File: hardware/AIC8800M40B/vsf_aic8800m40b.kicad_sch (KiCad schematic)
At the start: 87 parts, among them J1 USB_A, J2 USB_C_Receptacle_USB2.0, J3 USB_C_Receptacle_USB2.0, J4 Micro_SD_Card_Det1, J6 Conn_Coaxial, J7 Conn_Coaxial, J8 Conn_02x15_Odd_Even, Q1 S9013, SW1 SW_Push, SW2 SW_Push, SW3 SW_Push, SW4 SW_Push, U1 AIC8800MX0_48P, U2 CH340N, U3 ETA9638, U4 ETA3486, Y1 40M, 10PPM,10pF

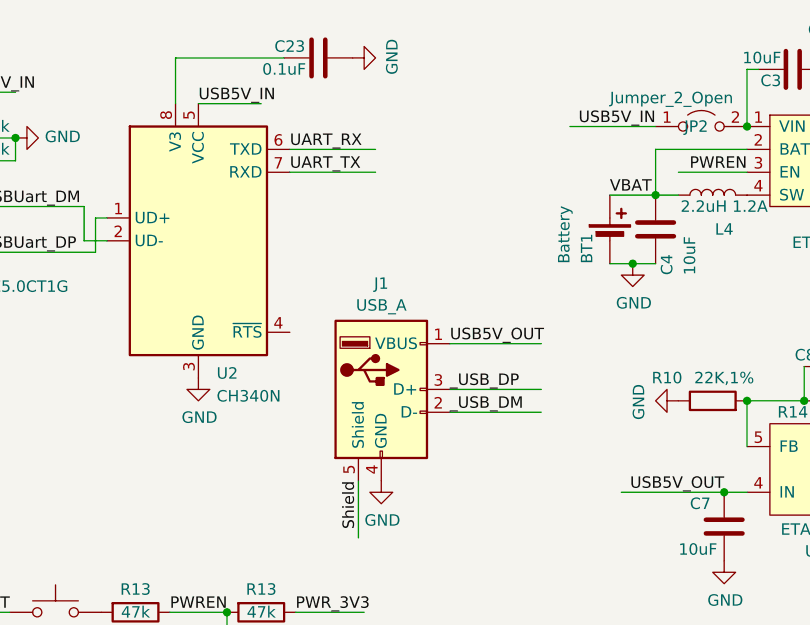
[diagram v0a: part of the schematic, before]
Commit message: [hardware/aic8800m40b] add level converter for debug uart
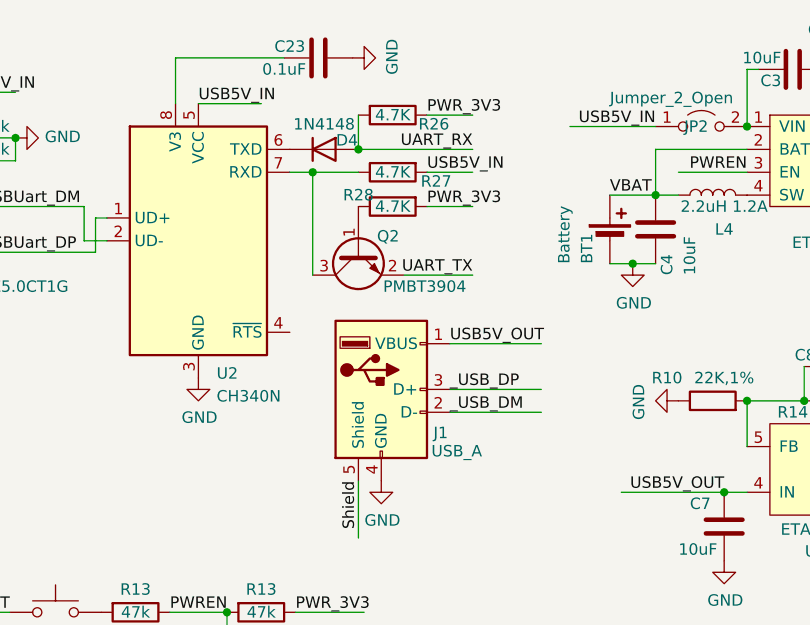
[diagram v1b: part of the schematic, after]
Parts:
- added D4: 1N4148, Diode_SMD:D_SOD-523, symbol Diode:1N4148
- added Q2: PMBT3904, Package_TO_SOT_SMD:SOT-23, symbol Device:Q_NPN_BEC
- added R26, R27, R28: 4.7K, Resistor_SMD:R_0402_1005Metric, symbol Device:R
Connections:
- net GPIOA8: now also D4.2 (A), R26.2; no longer U2.6 (TXD)
- net GPIOA9: now also Q2.2 (E); no longer U2.7 (RXD)
- net PWR_3V3: now also R26.1, R28.2
- net USB5V_IN: now also R27.2
- new net: Q2.3 (C), R27.1, U2.7 (RXD)
- new net: Q2.1 (B), R28.1
- new net: D4.1 (K), U2.6 (TXD)

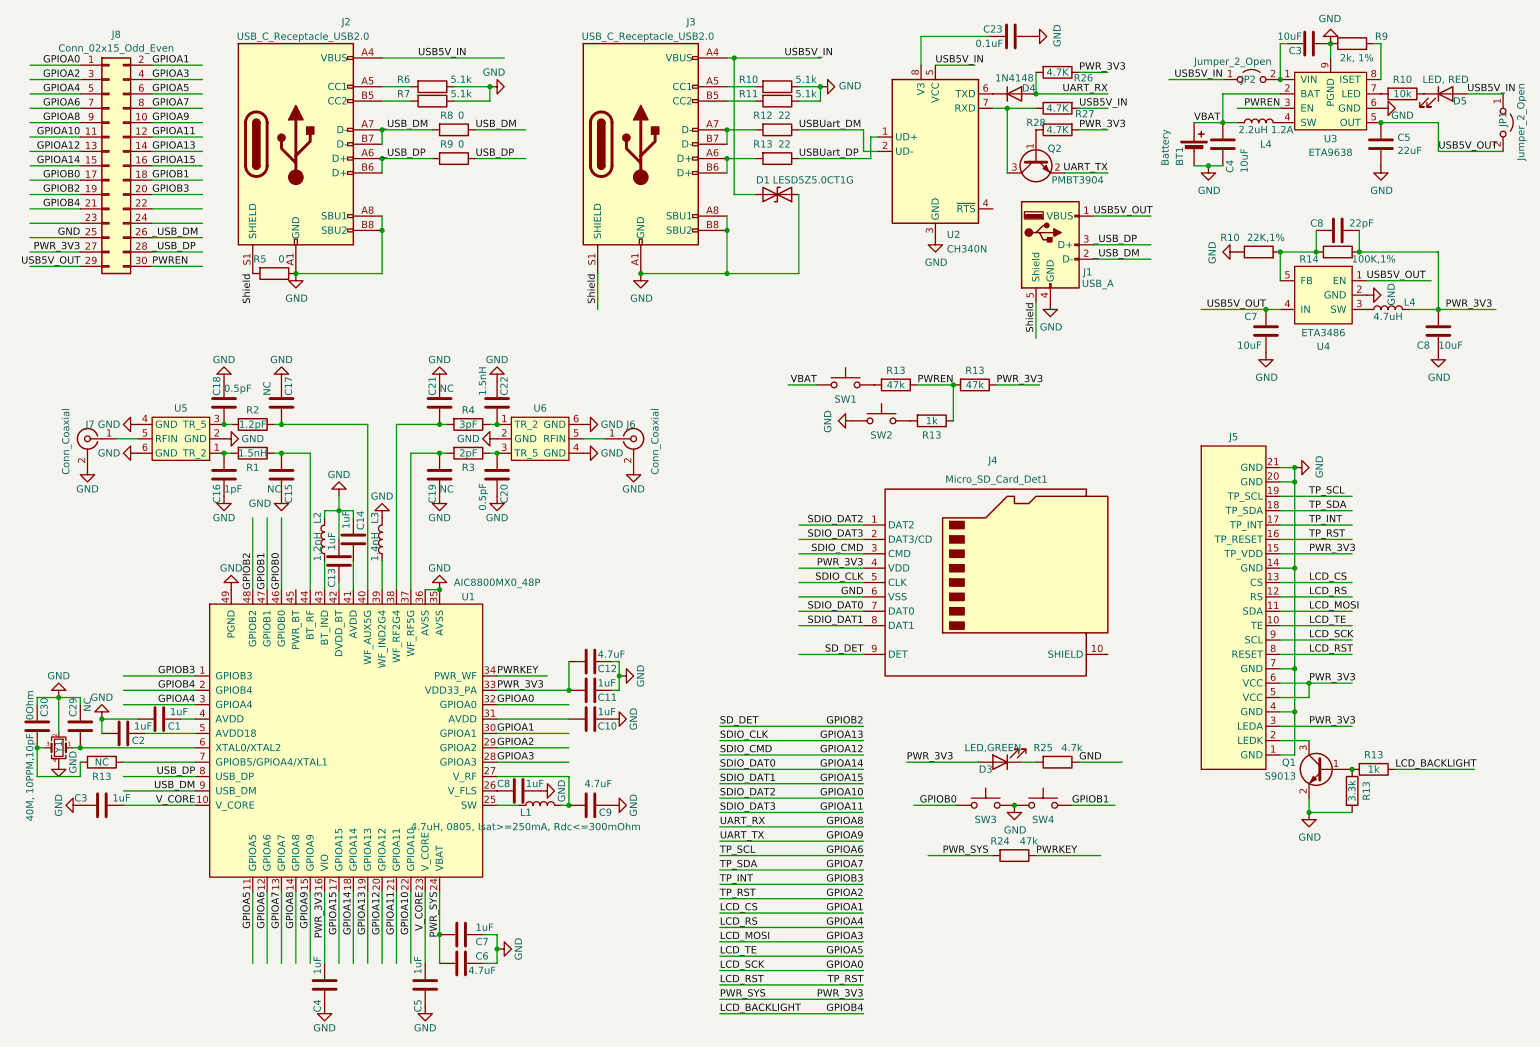
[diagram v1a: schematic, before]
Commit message: [hardware/aic8800m40b] fix typo
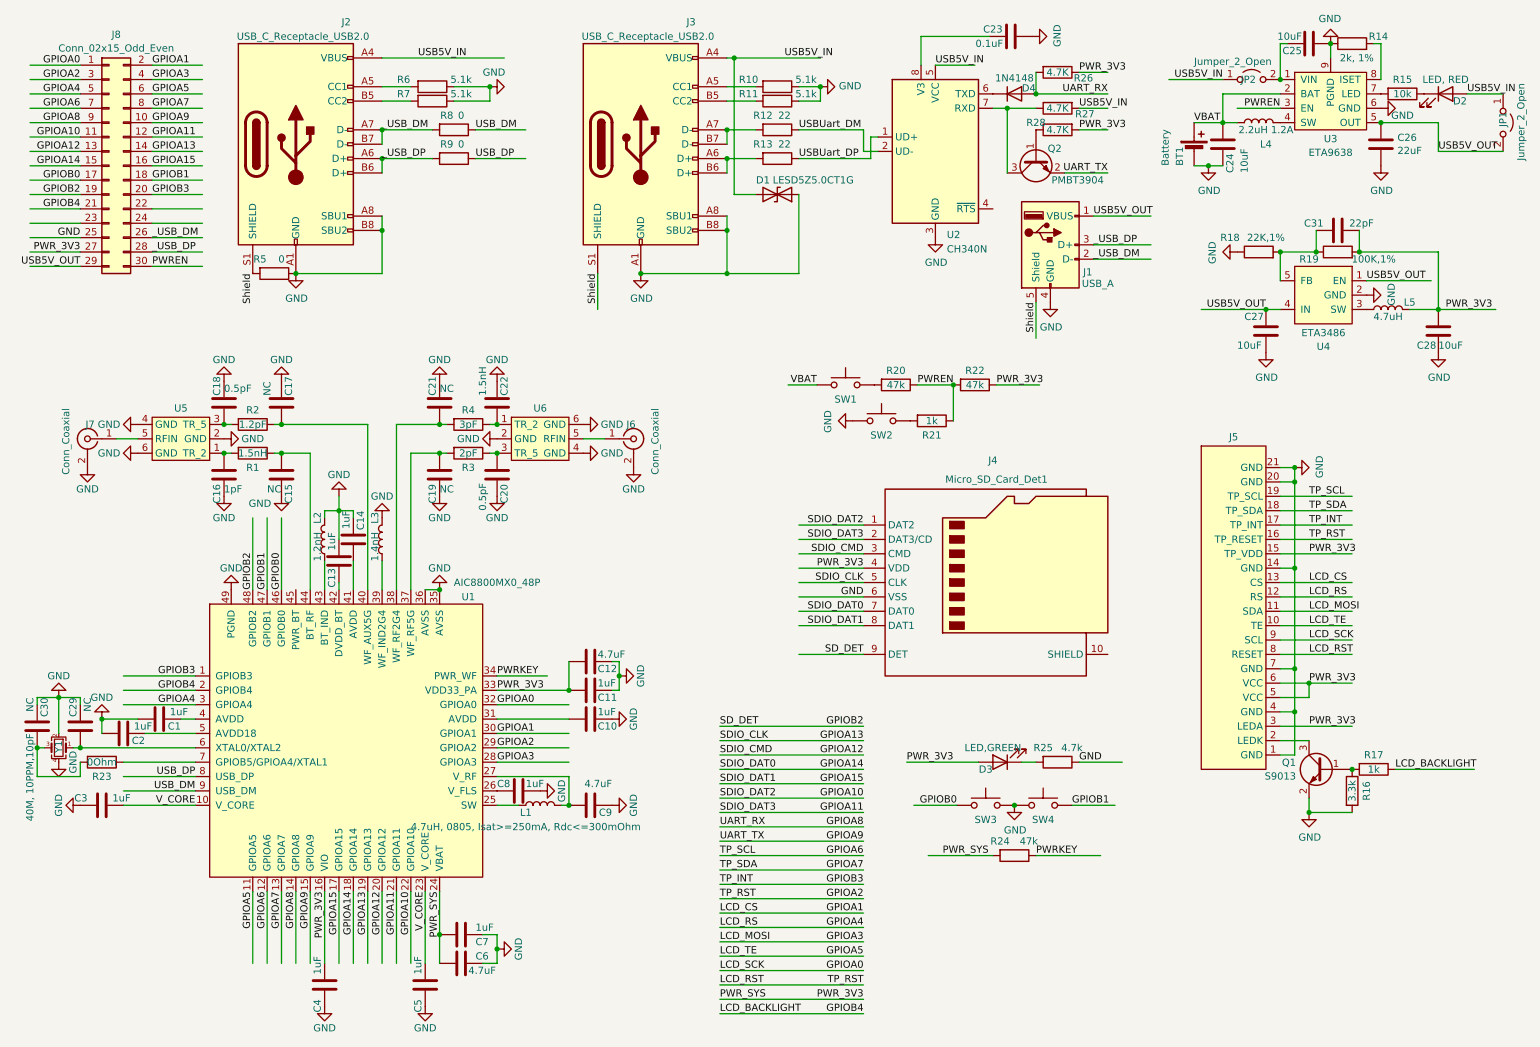
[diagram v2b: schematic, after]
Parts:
- C30: value 0Ohm -> NC
- R23: renamed from R13; value NC -> 0Ohm
- renumbered C4 to C24, C3 to C25, C5 to C26, C7 to C27, C8 to C28, C8 to C31, D5 to D2, L4 to L5, R9 to R14, R10 to R15, R13 to R16, R13 to R17, R10 to R18, R14 to R19, R13 to R20, R13 to R21, R13 to R22

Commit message: [hardware/aic8800m40b] update
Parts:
- D4: value 1N4148 -> PMEG1030EJ; footprint Diode_SMD:D_SOD-523 -> Diode_SMD:D_SOD-323
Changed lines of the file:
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@@
 			)
 		)
-		(property "Value" "1N4148"
-			(at 191.77 25.146 0)
+		(property "Value" "PMEG1030EJ"
+			(at 189.23 24.384 0)
 			(effects
 				(font
@@
 			)
 		)
-		(property "Footprint" "Diode_SMD:D_SOD-523"
+		(property "Footprint" "Diode_SMD:D_SOD-323"
 			(at 191.77 27.94 0)
 			(effects
